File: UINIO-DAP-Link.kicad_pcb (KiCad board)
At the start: 2 copper layers, 0 parts

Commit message: Update PCB.
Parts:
- added C1: 10nF, Capacitor_SMD:C_0603_1608Metric, F.Cu at (152.2, 92.6)
- added C2: 10uF, Capacitor_SMD:C_0603_1608Metric, F.Cu at (121.3, 112.0)
- added C3: 20pF, Capacitor_SMD:C_0603_1608Metric, F.Cu at (154.3, 95.1)
- added C4: 20pF, Capacitor_SMD:C_0603_1608Metric, F.Cu at (154.3, 97.6)
- added D1: Blue LED, Capacitor_SMD:C_0603_1608Metric, F.Cu at (164.4, 89.5)
- added D2: Blue LED, Capacitor_SMD:C_0603_1608Metric, F.Cu at (144.2, 108.6)
- added D3: BLUE LED, Capacitor_SMD:C_0603_1608Metric, F.Cu at (150.3, 102.2)
- added J1: Conn_01x05_Male, Connector_PinHeader_2.54mm:PinHeader_1x05_P2.54mm_Vertical, F.Cu at (128.9, 85.6)
- added J2: JTAG 输出, Connector_PinHeader_2.54mm:PinHeader_2x10_P2.54mm_Vertical, F.Cu at (121.7, 85.6)
- added J3: JTAG_nTRST 跳线选择, Connector_PinHeader_2.54mm:PinHeader_1x02_P2.54mm_Vertical, F.Cu at (160.1, 85.6)
- added J4: 3.3V 跳线选择, Connector_PinHeader_2.54mm:PinHeader_1x02_P2.54mm_Vertical, F.Cu at (139.9, 109.7)
- added J5: SWD 输入, Connector_PinHeader_2.54mm:PinHeader_2x05_P2.54mm_Vertical, F.Cu at (133.5, 85.6)
- added J6: DAPLink 固件下载接口, Connector:FanPinHeader_1x04_P2.54mm_Vertical, F.Cu at (147.9, 87.0)
- added J7: JTAG/SWD 下载接口, Connector_PinHeader_2.54mm:PinHeader_2x05_P2.54mm_Vertical, F.Cu at (140.7, 85.6)
- added R1: 1.5K, Resistor_SMD:R_0603_1608Metric, F.Cu at (150.3, 97.2)
- added R10: 10K, Resistor_SMD:R_0603_1608Metric, F.Cu at (158.3, 95.1)
- added R2: 1.5K, Resistor_SMD:R_0603_1608Metric, F.Cu at (160.2, 91.7)
- added R3: 1.5K, Resistor_SMD:R_0603_1608Metric, F.Cu at (168.4, 84.5)
- added R4: 22R, Resistor_SMD:R_0603_1608Metric, F.Cu at (154.3, 100.1)
- added R5: 22R, Resistor_SMD:R_0603_1608Metric, F.Cu at (156.2, 92.6)
- added R6: 10K, Resistor_SMD:R_0603_1608Metric, F.Cu at (164.4, 84.5)
- added R7: 10K, Resistor_SMD:R_0603_1608Metric, F.Cu at (150.3, 104.7)
- added R8: 10K, Resistor_SMD:R_0603_1608Metric, F.Cu at (164.4, 87.0)
- added R9: 100R, Resistor_SMD:R_0603_1608Metric, F.Cu at (150.3, 99.7)
- added U1: STM32F103C8T6, Uinio:LQFP-48_L7.0-W7.0-P0.50-LS9.0, F.Cu at (132.0, 103.6)
- added USB1: USB_Type_C_16Pin, Uinio:USB-C-SMD_TYPEC-304J-BCP16, F.Cu at (142.9, 101.7)
- added V1: ME6211, Uinio:SOT-23-5_L3.0-W1.7-P0.95-LS2.8-BR, F.Cu at (147.9, 93.5)
- added Y1: Crystal_GND24, Crystal:Crystal_SMD_0603-4Pin_6.0x3.5mm, F.Cu at (130.5, 111.8)

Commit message: Update PCB layout.
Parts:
- removed V1: ME6211, Uinio:SOT-23-5_L3.0-W1.7-P0.95-LS2.8-BR
- added C5: 0.1uF, Capacitor_SMD:C_0603_1608Metric, F.Cu at (52.3, 87.9)
- added D4: LED_Blue, LED_SMD:LED_0603_1608Metric, F.Cu at (56.8, 104.3)
- added D5: LED_Red, LED_SMD:LED_0603_1608Metric, F.Cu at (48.9, 104.3)
- added HOLE**: Hole-1mm, Uinio:Hole-1mm, F.Cu at (42.0, 91.7)
- added HOLE**: Hole-2mm, Uinio:Hole-2mm, F.Cu at (65.0, 104.2)
- added HOLE**: Hole-2mm, Uinio:Hole-2mm, F.Cu at (65.0, 88.0)
- added HOLE**: Hole-1mm, Uinio:Hole-1mm, F.Cu at (42.0, 100.4)
- added R11: 10K, Resistor_SMD:R_0603_1608Metric, F.Cu at (60.0, 104.3)
- added R12: 10K, Resistor_SMD:R_0603_1608Metric, F.Cu at (50.7, 104.3)
- added U2: STM32F103C8T6, Uinio:LQFP-48_L7.0-W7.0-P0.50-LS9.0, F.Cu at (49.8, 96.2)
- D1: value Blue LED -> LED_Red; footprint Capacitor_SMD:C_0603_1608Metric -> LED_SMD:LED_0603_1608Metric
- D2: value Blue LED -> LED_Blue; footprint Capacitor_SMD:C_0603_1608Metric -> LED_SMD:LED_0603_1608Metric
- D3: value BLUE LED -> LED_Blue; footprint Capacitor_SMD:C_0603_1608Metric -> LED_SMD:LED_0603_1608Metric
- J1: value Conn_01x05_Male -> 扩展板串口 & 电源输出
- J2: value JTAG 输出 -> 扩展板 JTAG 输出; footprint Connector_PinHeader_2.54mm:PinHeader_2x10_P2.54mm_Vertical -> Connector_IDC:IDC-Header_2x10_P2.54mm_Horizontal
- J5: value SWD 输入 -> 扩展板 SWD 输入; footprint Connector_PinHeader_2.54mm:PinHeader_2x05_P2.54mm_Vertical -> Connector_IDC:IDC-Header_2x05_P2.54mm_Horizontal
- J6: footprint Connector:FanPinHeader_1x04_P2.54mm_Vertical -> Connector_PinHeader_2.54mm:PinHeader_1x04_P2.54mm_Vertical
- J7: footprint Connector_PinHeader_2.54mm:PinHeader_2x05_P2.54mm_Vertical -> Connector_IDC:IDC-Header_2x05_P2.54mm_Horizontal
- U1: value STM32F103C8T6 -> ME6211; footprint Uinio:LQFP-48_L7.0-W7.0-P0.50-LS9.0 -> Uinio:SOT-23-5_L3.0-W1.7-P0.95-LS2.8-BR
- moved R8 117.1 mm to (47.3, 87.9), turned to -90 degrees
- moved R6 113.8 mm to (50.7, 87.9), turned to 90 degrees
- moved J6 113.1 mm to (36.2, 105.1), turned to 90 degrees
- moved C1 110.5 mm to (41.7, 89.4), turned to 180 degrees
- moved R9 108.2 mm to (42.2, 96.2)
- moved USB1 106.1 mm to (36.9, 96.1), turned to -90 degrees
- moved R7 102.7 mm to (49.0, 87.9), turned to 90 degrees
- moved R10 100.3 mm to (58.4, 104.3), turned to -90 degrees
- moved U1 95.4 mm to (37.8, 88.4), turned to 180 degrees
- moved C4 94.4 mm to (60.5, 87.9), turned to 90 degrees
- moved C3 93.9 mm to (60.5, 91.7), turned to -90 degrees
- moved C2 83.3 mm to (41.7, 87.4)
- moved J7 77.3 mm to (63.7, 91.1)
- moved Y1 76.4 mm to (57.4, 89.8), turned to -90 degrees
- moved J3 56.8 mm to (108.2, 108.7)
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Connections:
- R6 pad 1: /JTAG_nTRST -> Net-(C5-Pad1)
- R7 pad 1: /BOOT1 -> /JTAG_nTRST
- R7 pad 2: GND -> /VDD_3.3V
- R8 pad 1: Net-(R8-Pad1) -> /BOOT1
- R8 pad 2: /VDD_3.3V -> GND
- U1 pad 1: /VDD_3.3V -> /VDD_5V
- U1 pad 2: unconnected-(U1-Pad2) -> GND
- U1 pad 3: unconnected-(U1-Pad3) -> /VDD_5V
- U1 pad 4: unconnected-(U1-Pad4) -> Net-(C1-Pad2)
- U1 pad 5: Net-(U1-Pad5) -> /VDD_3.3V
- Y1 pad 1: Net-(U1-Pad6) -> Net-(U2-Pad6)
- Y1 pad 3: Net-(U1-Pad5) -> Net-(U2-Pad5)
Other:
- board outline added: 135.6 x 36.3 mm

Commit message: Update PCB layout.
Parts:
- removed HOLE** (x2): Hole-1mm, Uinio:Hole-1mm
- removed HOLE** (x2): Hole-2mm, Uinio:Hole-2mm
- moved J4 35.4 mm to (106.2, 111.0), turned to 90 degrees
- moved J1 34.3 mm to (105.2, 80.5), turned to 90 degrees
- moved J2 30.6 mm to (122.1, 84.6)
- moved R5 27.5 mm to (108.8, 107.2)
- moved R4 27.5 mm to (108.8, 103.9)
- moved R3 11.9 mm to (108.8, 97.3)
- moved R2 11.8 mm to (108.8, 94.0)
- moved R9 10.3 mm to (48.1, 104.5), turned to 90 degrees
- moved R1 8.98 mm to (108.8, 84.1)
- moved J5 8.72 mm to (103.2, 101.2)
- moved D1 7.73 mm to (108.8, 87.4)
- moved J3 6.45 mm to (114.1, 111.2), turned to 90 degrees
- moved D3 2.85 mm to (108.8, 100.6)
- moved D2 1.29 mm to (108.8, 90.7)
- moved D5 0.98 mm to (49.9, 104.5)
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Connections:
- J2 pad 11: /3.3V_Output -> /VTref
- J2 pad 3: /TDI -> /_JTAG_TDI
- J2 pad 4: /TMS -> /_JTAG_TMS/SWDIO
- J2 pad 5: /TCK -> /_JTAG_TCK/SWCLK
- J2 pad 7: /TDO -> /_JTAG_TDO
- J2 pad 8: /RESET -> /_JTAG_nTRST_Output
- J4 pad 2: /3.3V_Output -> /VTref
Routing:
- net /JTAG_TMS/SWDIO: track 0.00 -> 0.77 mm
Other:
- board size 135.6 x 36.3 mm -> 100.7 x 33.3 mm

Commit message: Update PCB layout.
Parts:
- added HOLE**: Hole-1mm, Uinio:Hole-1mm, F.Cu at (33.5, 105.0)
- added HOLE**: Hole-2mm, Uinio:Hole-2mm, F.Cu at (116.4, 83.6)
- added HOLE**: Hole-2mm, Uinio:Hole-2mm, F.Cu at (116.4, 108.7)
- added HOLE**: Hole-1mm, Uinio:Hole-1mm, F.Cu at (33.5, 87.2)
- added HOLE**: Hole-2mm, Uinio:Hole-2mm, F.Cu at (98.5, 108.7)
- added HOLE**: Hole-2mm, Uinio:Hole-2mm, F.Cu at (64.0, 88.0)
- added HOLE**: Hole-2mm, Uinio:Hole-2mm, F.Cu at (98.5, 83.6)
- added HOLE**: Hole-2mm, Uinio:Hole-2mm, F.Cu at (64.0, 104.2)
- moved R1 17.5 mm to (112.0, 101.3), turned to 180 degrees
- moved D1 13.9 mm to (108.2, 101.3), turned to 180 degrees
- moved R5 10.8 mm to (108.2, 96.4), turned to 180 degrees
- moved D3 9.51 mm to (108.1, 91.1), turned to 180 degrees
- moved R3 6.92 mm to (111.9, 91.1)
- moved R4 5.75 mm to (108.2, 98.2), turned to 180 degrees
- moved J3 4.90 mm to (110.0, 108.6)
- moved J4 4.50 mm to (102.4, 108.6)
- moved J1 4.27 mm to (102.4, 83.7)
- moved R2 3.19 mm to (111.9, 93.3)
- moved D2 2.65 mm to (108.1, 93.3), turned to 180 degrees
- moved J2 2.36 mm to (119.8, 84.6)
- moved J5 2.36 mm to (100.9, 101.2)
- moved R12 1.66 mm to (50.0, 104.5)
- moved D5 1.66 mm to (48.2, 104.5)
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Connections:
- net /VTref renamed /3.3V_Output
- J5 pad 1: Net-(J5-Pad1) -> /_USART2_TX
- J5 pad 10: /_JTAG_TCK/SWCLK -> /_VDD_5V
- J5 pad 2: Net-(J5-Pad2) -> /_JTAG_TCK/SWCLK
- J5 pad 3: /_JTAG_nTRST_Output -> /_USART2_RX
- J5 pad 4: /_USART2_RX -> GND
- J5 pad 5: /_USART2_TX -> /_JTAG_nTRST_Output
- J5 pad 6: /_VDD_5V -> /_JTAG_TMS/SWDIO
- J5 pad 7: /_VDD_3.3V -> Net-(R4-Pad2)
- J5 pad 8: /_JTAG_TMS/SWDIO -> /_VDD_3.3V
- J5 pad 9: GND -> Net-(R5-Pad2)
- J7 pad 1: /USART2_TX -> /JTAG_TDI
- J7 pad 10: /VDD_5V -> /JTAG_TCK/SWCLK
- J7 pad 2: /USART2_RX -> /VDD_5V
- J7 pad 3: /JTAG_nTRST -> /JTAG_TDO
- J7 pad 4: /JTAG_TDO -> /VDD_3.3V
- J7 pad 5: /JTAG_TDI -> /JTAG_nTRST
- J7 pad 6: /JTAG_TCK/SWCLK -> /JTAG_TMS/SWDIO
- J7 pad 7: GND -> /USART2_RX
- J7 pad 8: /JTAG_TMS/SWDIO -> GND
- J7 pad 9: /VDD_3.3V -> /USART2_TX
- R4 pad 2: Net-(J5-Pad2) -> Net-(R4-Pad2)
- R5 pad 2: Net-(J5-Pad1) -> Net-(R5-Pad2)
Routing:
- net unconnected-(U2-Pad29): track 0.00 -> 0.77 mm
- net /JTAG_TMS/SWDIO: track 0.77 -> 0.00 mm
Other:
- board size 100.7 x 33.3 mm -> 99.1 x 31 mm

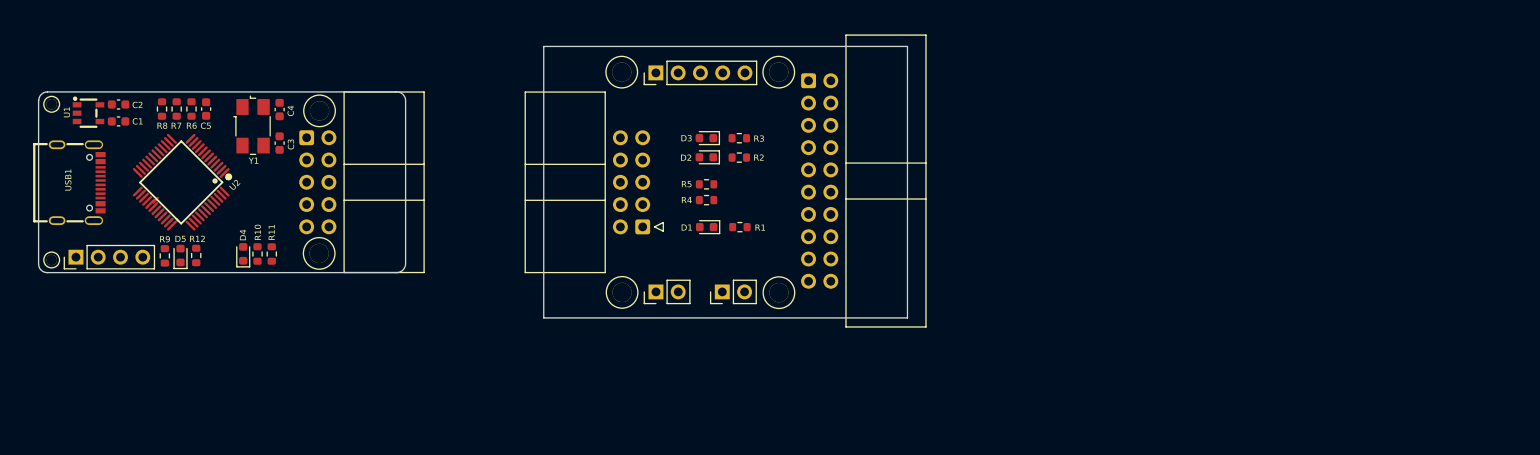
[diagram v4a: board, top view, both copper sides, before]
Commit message: Preliminarily completed the PCB layout.
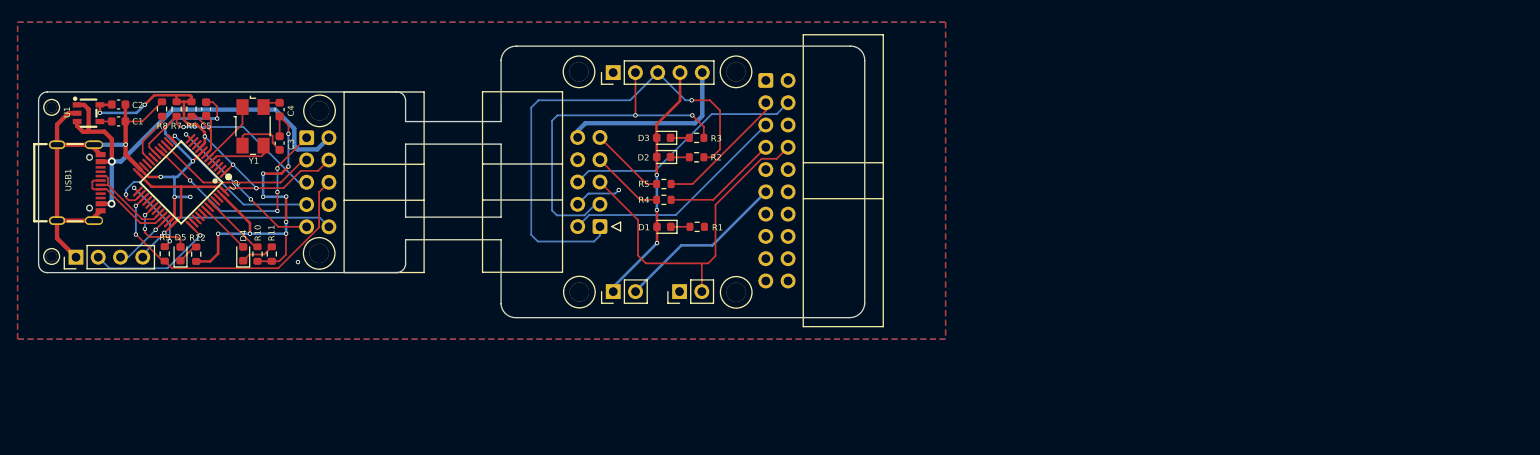
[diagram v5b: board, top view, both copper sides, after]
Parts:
- moved D1 4.87 mm to (103.3, 101.2)
- moved HOLE5 4.87 mm to (93.6, 83.5)
- moved HOLE6 4.87 mm to (93.7, 108.7)
- moved HOLE7 4.87 mm to (111.5, 108.7)
- moved HOLE8 4.87 mm to (111.5, 83.5)
- moved J1 4.87 mm to (97.5, 83.6)
- moved J2 4.87 mm to (114.9, 84.5)
- moved J3 4.87 mm to (105.1, 108.6)
- moved J5 4.87 mm to (96.0, 101.2)
- moved R1 4.87 mm to (107.1, 101.2)
- moved R2 4.87 mm to (107.0, 93.3)
- moved R3 4.87 mm to (107.0, 91.1)
- moved R4 4.87 mm to (103.3, 98.1)
- moved R5 4.87 mm to (103.3, 96.3)
- moved D2 4.87 mm to (103.3, 93.3)
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- renumbered HOLE** to HOLE1, HOLE** to HOLE2, HOLE** to HOLE3, HOLE** to HOLE4, HOLE** to HOLE5, HOLE** to HOLE6, HOLE** to HOLE7, HOLE** to HOLE8
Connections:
- J1 pad 5: /5V -> /_VDD_5V
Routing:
- net GND: track 0.00 -> 128.4 mm, vias 0 -> 17
- net /VDD_3.3V: track 0.00 -> 67.0 mm, vias 0 -> 6
- net /_USART2_TX: track 0.00 -> 55.6 mm, vias 0 -> 1
- net /VDD_5V: track 0.00 -> 50.0 mm, vias 0 -> 2
- net /_USART2_RX: track 0.00 -> 40.2 mm, vias 0 -> 2
- net /_JTAG_nTRST_Output: track 0.00 -> 39.8 mm
- net /JTAG_TMS/SWDIO: track 0.00 -> 34.4 mm, vias 0 -> 2
- net /JTAG_TCK/SWCLK: track 0.00 -> 28.6 mm, vias 0 -> 1
- net /_JTAG_TMS/SWDIO: track 0.00 -> 27.7 mm
- net /3.3V_Input: track 0.00 -> 27.5 mm, vias 0 -> 3
- net /_JTAG_TCK/SWCLK: track 0.00 -> 26.2 mm
- net /JTAG_TDI: track 0.00 -> 26.0 mm, vias 0 -> 4
- net /JTAG_nTRST: track 0.00 -> 24.4 mm, vias 0 -> 1
- net /_VDD_5V: track 0.00 -> 20.6 mm
- net /3.3V_Output: track 0.00 -> 19.5 mm
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- added copper zone on B.Cu, net GND
- added copper zone on F.Cu, net GND
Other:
- board size 99.1 x 31 mm -> 94.2 x 31 mm

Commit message: Release UINIO-DAP-Link 1.0.0.
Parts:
- added ?: , LOGO, F.Cu at (182.6, 107.7)
- added ?: , LOGO, F.Cu at (127.8, 110.6)
- added ?: , LOGO, B.Cu at (120.5, 107.4)
- added ?: , LOGO, B.Cu at (175.1, 107.2)
- moved R5 71.7 mm to (174.1, 107.8)
- moved R4 71.7 mm to (174.1, 109.5)
- moved D1 71.7 mm to (174.1, 112.7)
- moved D2 71.7 mm to (174.0, 104.5)
- moved D3 71.7 mm to (174.0, 102.3)
- moved R1 71.6 mm to (177.8, 112.7)
- moved HOLE5 71.6 mm to (164.3, 94.8)
- moved J2 71.6 mm to (185.6, 95.8)
- moved J7 71.6 mm to (133.2, 102.3)
- moved R12 71.6 mm to (120.7, 115.6)
- moved R2 71.6 mm to (177.7, 104.5)
- moved R3 71.6 mm to (177.7, 102.3)
- moved D4 71.6 mm to (126.0, 115.6)
- moved D5 71.6 mm to (118.9, 115.6)
- moved HOLE1 71.6 mm to (104.2, 98.9)
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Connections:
- net /_JTAG_nTRST_Input renamed /_JTAG_nSRST_Input
- J1 pad 1: GND -> /_USART2_RX
- J1 pad 2: /_USART2_RX -> /_USART2_TX
- J1 pad 3: /_USART2_TX -> /3.3V_Input
- J1 pad 4: /3.3V_Input -> GND
- J2 pad 10: unconnected-(J2-Pad10) -> GND
- J2 pad 11: /3.3V_Output -> /RTCK
- J2 pad 13: GND -> /_JTAG_TDO
- J2 pad 15: GND -> /_JTAG_nSRST_Output
- J2 pad 17: GND -> unconnected-(J2-Pad17)
- J2 pad 19: GND -> unconnected-(J2-Pad19)
- J2 pad 2: /nTRST -> /3.3V_Output
- J2 pad 3: /_JTAG_TDI -> /nTRST
- J2 pad 4: /_JTAG_TMS/SWDIO -> GND
- J2 pad 5: /_JTAG_TCK/SWCLK -> /_JTAG_TDI
- J2 pad 6: /RTCK -> GND
- J2 pad 7: /_JTAG_TDO -> /_JTAG_TMS/SWDIO
- J2 pad 8: /_JTAG_nTRST_Output -> GND
- J2 pad 9: unconnected-(J2-Pad9) -> /_JTAG_TCK/SWCLK
- J3 pad 2: /_JTAG_nTRST_Output -> /_JTAG_nSRST_Output
- J5 pad 2: /_JTAG_TCK/SWCLK -> GND
- J5 pad 4: GND -> /_JTAG_TCK/SWCLK
- J5 pad 5: /_JTAG_nTRST_Output -> /_JTAG_nSRST_Output
- J7 pad 10: /JTAG_TCK/SWCLK -> GND
- J7 pad 8: GND -> /JTAG_TCK/SWCLK
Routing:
- net GND: track 128.4 -> 179.7 mm, vias 17 -> 24
- net /_JTAG_nTRST_Output: track 39.8 -> 0.00 mm
- net /_JTAG_nSRST_Output: track 0.00 -> 28.6 mm
- net /3.3V_Output: track 19.5 -> 33.6 mm
- net /_JTAG_TMS/SWDIO: track 27.7 -> 23.1 mm, vias 0 -> 1
- net /_JTAG_TCK/SWCLK: track 26.2 -> 23.1 mm, vias 0 -> 1
- net /_JTAG_TDO: track 13.3 -> 11.2 mm
- net Net-(R9-Pad2): track 9.18 -> 11.2 mm
- net /_JTAG_TDI: track 15.2 -> 13.6 mm
- net /VDD_3.3V: track 67.0 -> 68.5 mm
- net /3.3V_Input: track 27.5 -> 26.3 mm
- net Net-(D5-Pad2): track 8.49 -> 7.95 mm
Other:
- board text added: "3.3V"
- board text added: "3.3V跳线"
- board text added: "5V"
- board text added: "GND"
- board text added: "RX"
- board text added: "SWCLK"
- board text added: "SWDIO"
- board text added: "TCK"
- board text added: "TDI"
- board text added: "TDO"
- board text added: "TMS"
- board text added: "TX"
- board text added: "UINIO-DAP-Link"
- board text added: "Version 1.0.0"
- board text added: "X"
- board text added: "nSRST"
- board text added: "nSRST跳线"
- board text added: "nTRST"

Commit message: Release UINIO-DAP-Link 1.0.0.
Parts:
- moved ? 0.25 mm to (182.6, 107.4)
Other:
- board text added: "JTAG接口"
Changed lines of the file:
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@@
   )
   (footprint "LOGO" (layer "F.Cu")
-    (at 182.58 107.65 -90)
+    (at 182.55 107.4 -90)
     (attr board_only exclude_from_pos_files exclude_from_bom)
     (fp_text reference "" (at 0 0 90) (layer "F.SilkS")
@@
     (effects (font (size 1 1) (thickness 0.2)))
   )
+  (gr_text "JTAG接口" (at 169.39 115.49) (layer "F.SilkS")
+    (effects (font (size 1 1) (thickness 0.1)))
+  )
+  (gr_text "JTAG接口" (at 177.32 115.49) (layer "F.SilkS")
+    (effects (font (size 1 1) (thickness 0.1)))
+  )
   (gr_text "3.3V跳线" (at 169.43 117.07) (layer "F.SilkS")

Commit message: Release UINIO-DAP-Link 1.0.0.
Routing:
- net /3.3V_Input: track 26.3 -> 27.4 mm
- net /VDD_5V: track 50.0 -> 50.6 mm
- net GND: track 179.7 -> 179.1 mm, vias 24 -> 25
